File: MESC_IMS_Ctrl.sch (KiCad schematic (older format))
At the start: 78 parts, among them J1 Conn_01x08_Female, J10 Conn_01x04_Male, J2 Conn_01x08_Female, J3 Conn_01x08_Female, J4 Conn_01x06_Male, J5 Conn_ARM_JTAG_SWD_10, J6 USB_C_Receptacle_USB2.0, J7 Conn_01x03_Male, J8 Conn_01x04_Male, J9 Conn_01x08_Male, U1 STM32F303CBTx, Y1 ASE-8.000MHZ-LC-T

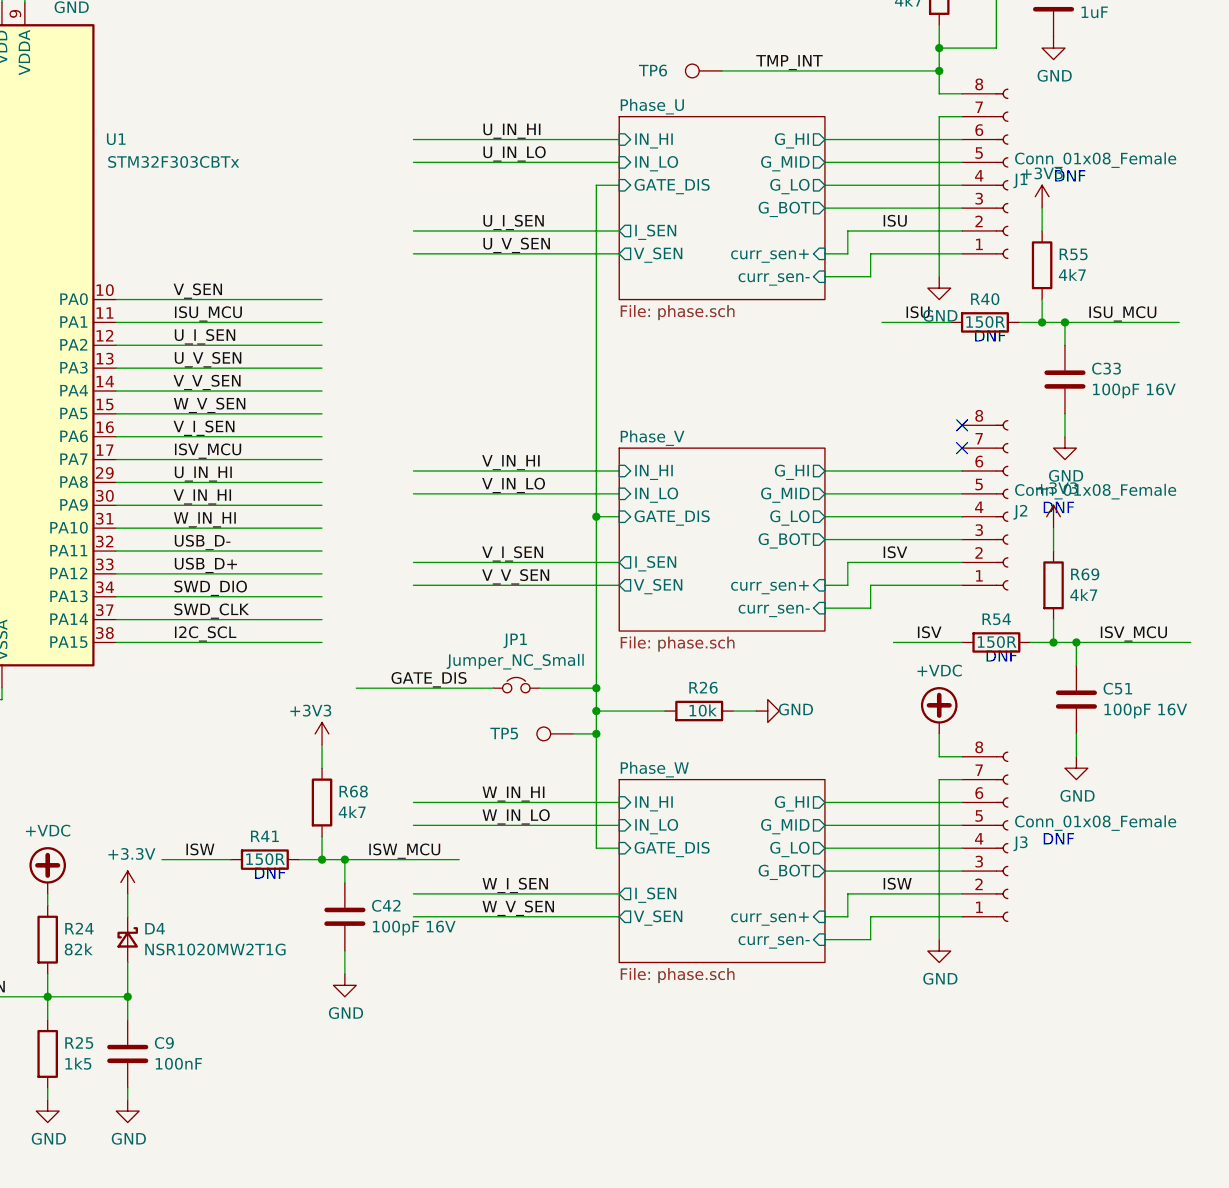
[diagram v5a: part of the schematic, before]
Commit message: Cleaned up the schematic
Also regenerated the pdf & set boot diodes to SOD128.
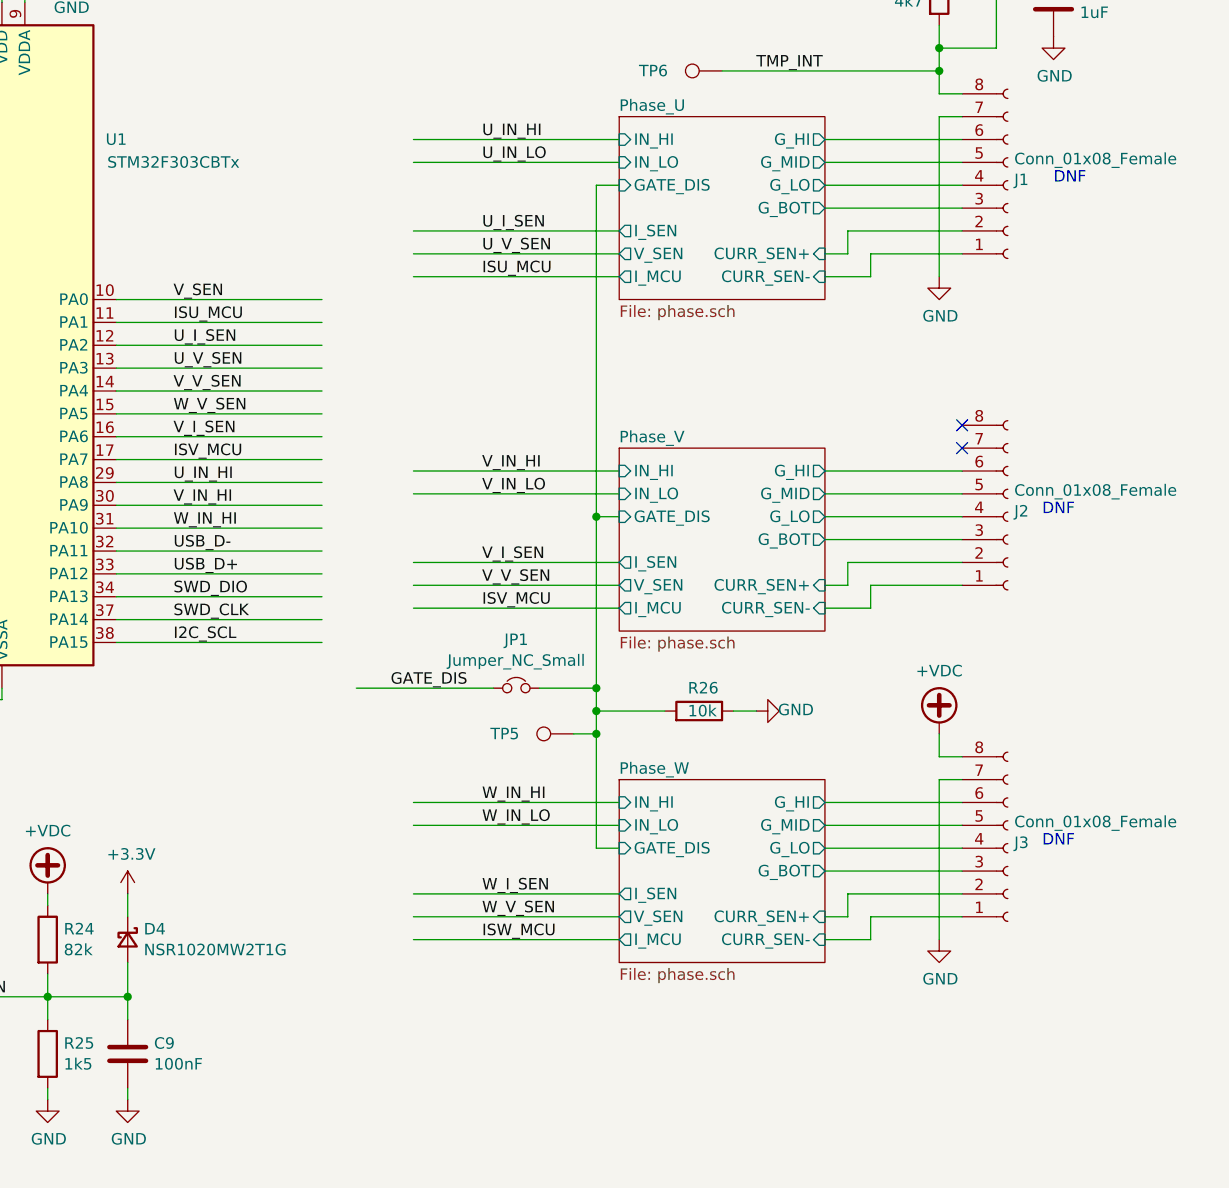
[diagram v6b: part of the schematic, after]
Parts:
- removed C33, C42, C51: 100pF 16V, Capacitor_SMD:C_0402_1005Metric, symbol Device:C
- removed R40, R41, R54: 150R, Resistor_SMD:R_0402_1005Metric, symbol Device:R
- removed R55, R68, R69: 4k7, Resistor_SMD:R_0402_1005Metric, symbol Device:R
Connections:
- net labels removed: ISU, ISV, ISW
- wire segments 309 -> 288

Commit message: Initial gate driver placement/routing
Also adding images to README
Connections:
- net labels added: CLK
- net labels removed: SWO
- wire segments 288 -> 287
- no-connect marks 9 -> 10
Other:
- moved on the sheet: H3
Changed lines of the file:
@@
 Wire Wire Line
 	1500 6650 2000 6650
-Wire Wire Line
-	1500 6750 2000 6750
-Text Label 1650 6750 0    50   ~ 0
-SWO
 Text Label 1650 6650 0    50   ~ 0
 SWD_DIO
@@
 L Mechanical:MountingHole H3
 U 1 1 60792780
-P 6300 7350
-F 0 "H3" H 6400 7396 50  0000 L CNN
-F 1 "MountingHole" H 6400 7305 50  0000 L CNN
-F 2 "MountingHole:MountingHole_3.2mm_M3_Pad_Via" H 6300 7350 50  0001 C CNN
-F 3 "~" H 6300 7350 50  0001 C CNN
-F 4 "~" H 6300 7350 50  0001 C CNN "LCSC"
-	1    6300 7350
+P 6300 7400
+F 0 "H3" H 6400 7446 50  0000 L CNN
+F 1 "MountingHole" H 6400 7355 50  0000 L CNN
+F 2 "MountingHole:MountingHole_3.2mm_M3_Pad_Via" H 6300 7400 50  0001 C CNN
+F 3 "~" H 6300 7400 50  0001 C CNN
+F 4 "~" H 6300 7400 50  0001 C CNN "LCSC"
+	1    6300 7400
 	1    0    0    -1
 $EndComp
@@
 Wire Wire Line
 	7750 4700 8650 4700
+NoConn ~ 1500 6750
+Text Label 4700 2650 0    50   ~ 0
+CLK
 $EndSCHEMATC

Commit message: Some more routing
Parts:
- J9: footprint Connector_JST:JST_PH_B8B-PH-SM4-TB_1x08-1MP_P2.00mm_Vertical -> Connector_JST:JST_PH_S8B-PH-SM4-TB_1x08-1MP_P2.00mm_Horizontal
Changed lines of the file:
@@
 F 0 "J9" H 3058 7181 50  0000 C CNN
 F 1 "Conn_01x08_Male" V 2900 6650 50  0000 C CNN
-F 2 "Connector_JST:JST_PH_B8B-PH-SM4-TB_1x08-1MP_P2.00mm_Vertical" H 2950 6700 50  0001 C CNN
+F 2 "Connector_JST:JST_PH_S8B-PH-SM4-TB_1x08-1MP_P2.00mm_Horizontal" H 2950 6700 50  0001 C CNN
 F 3 "~" H 2950 6700 50  0001 C CNN
 F 4 "~" H 2950 6700 50  0001 C CNN "LCSC"
